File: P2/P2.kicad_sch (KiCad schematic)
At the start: 16 parts, among them J1 Power, J2 Digital/PWM, J3 Analog, J4 Digital/PWM, SW1 SW_Rotary_2x6, U2 LM393

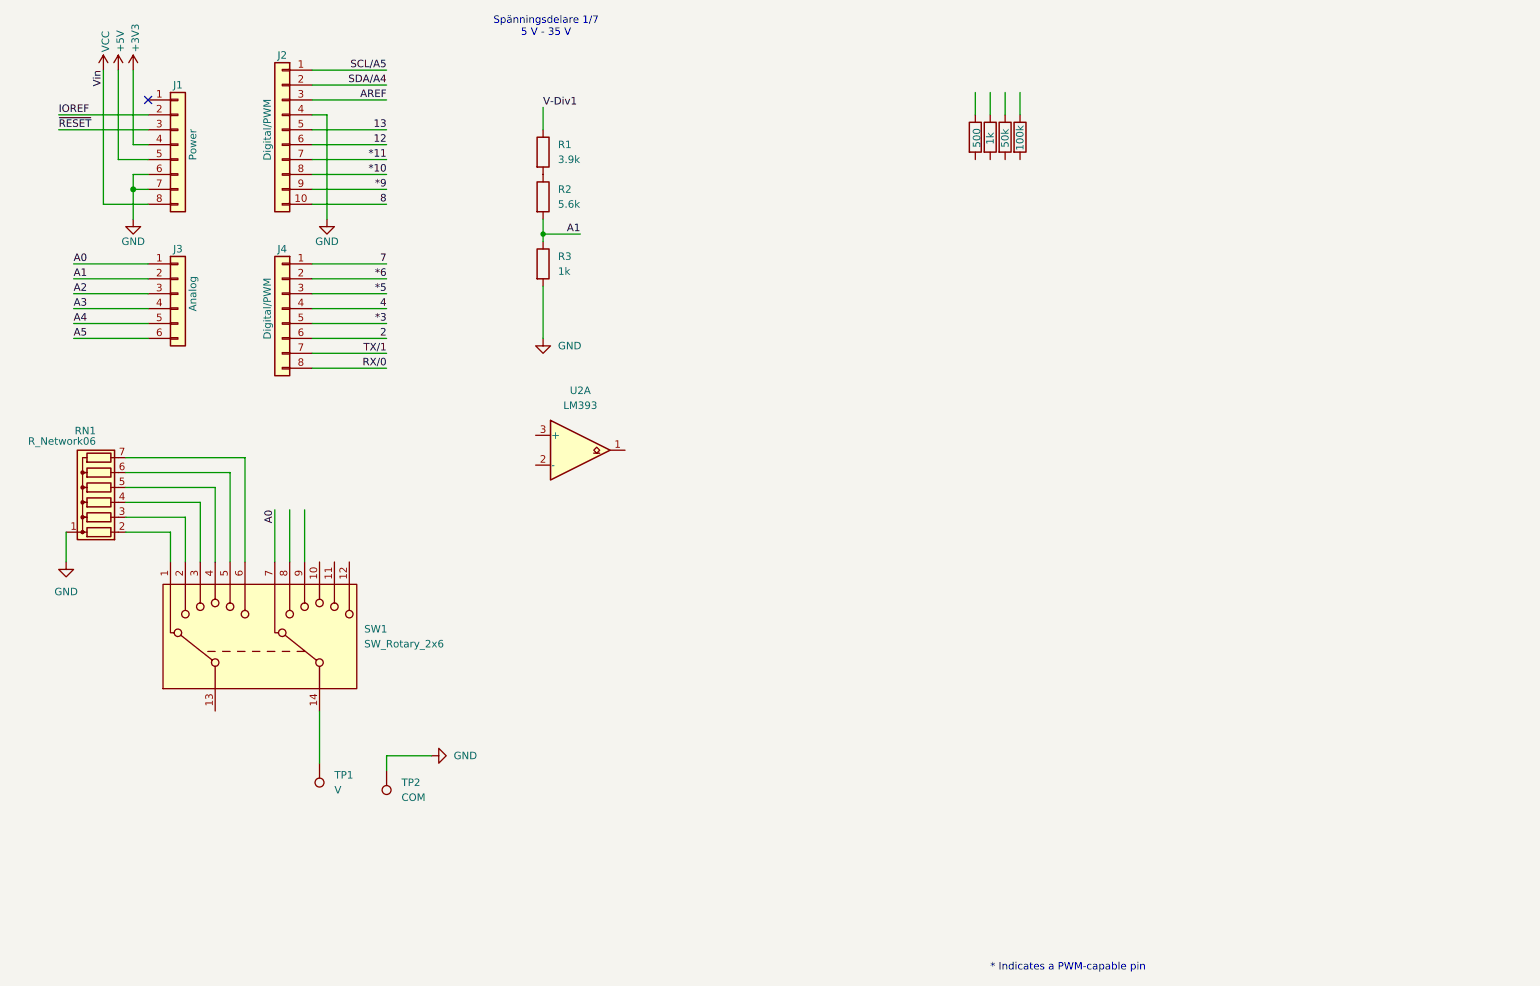
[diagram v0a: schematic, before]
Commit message: Adds rounding and formatting data for P2
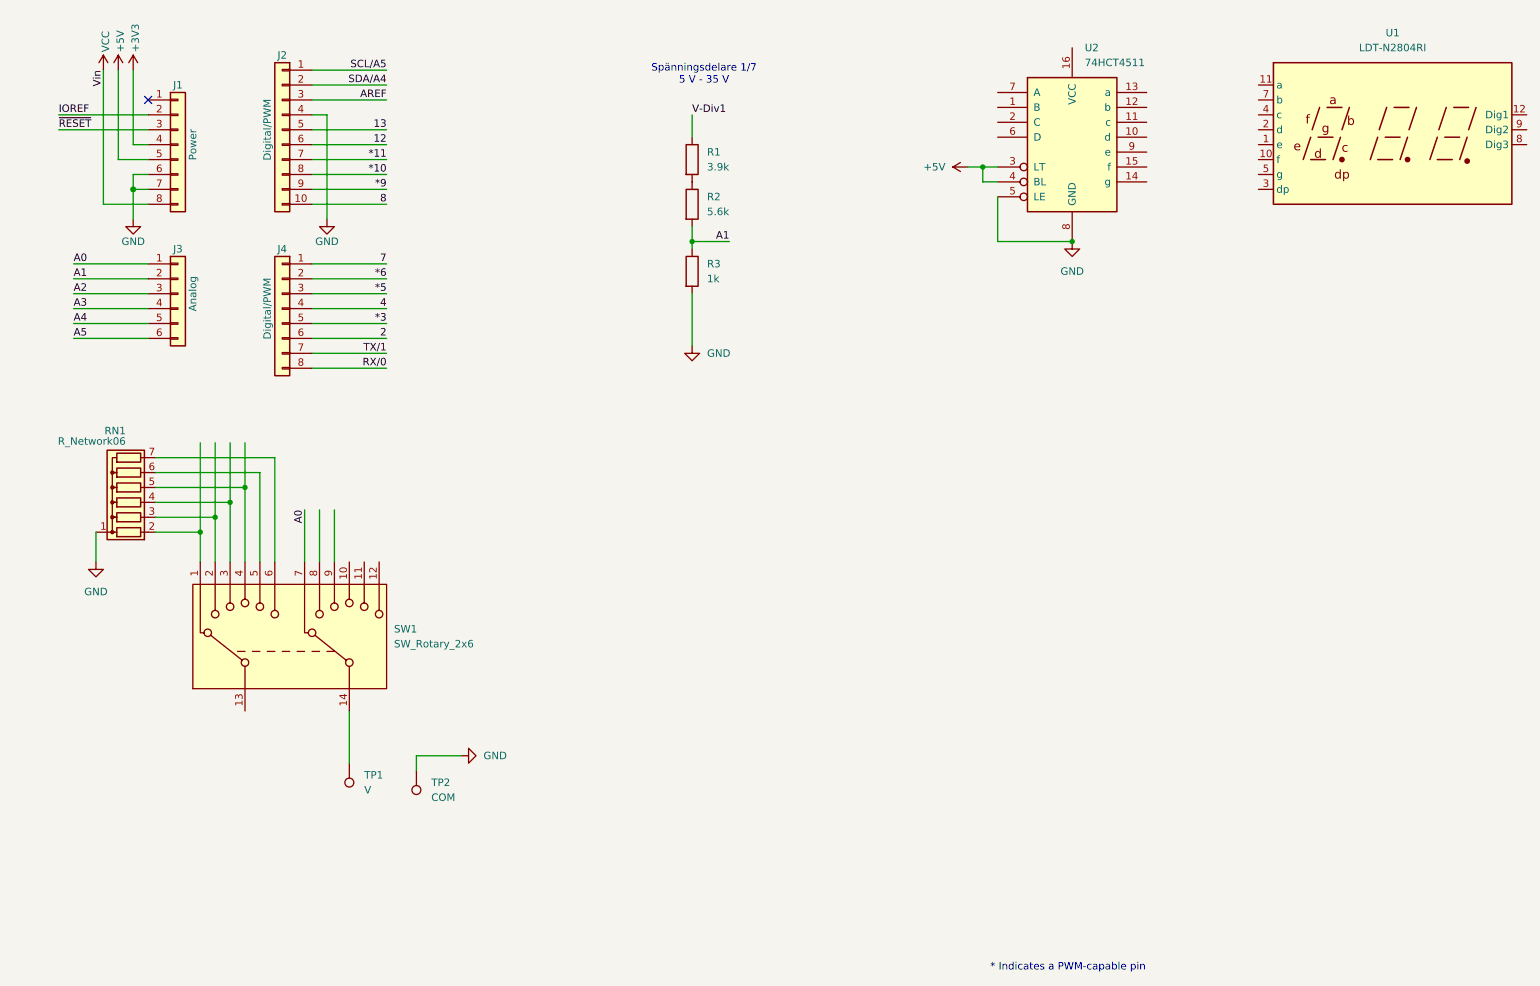
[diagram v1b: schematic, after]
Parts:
- removed R4: 500, symbol Device:R
- removed R5: 1k, symbol Device:R
- removed R6: 50k, symbol Device:R
- removed R7: 100k, symbol Device:R
- removed U2: LM393, symbol Comparator:LM393
- added U1: LDT-N2804RI, Display_7Segment:CA56-12SRWA, symbol joel_library:LDT-N2804RI
- added U2: 74HCT4511, symbol joel_library:74HCT4511
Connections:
- net +5V: now also U2.3 (LT), U2.4 (BL)
- net GND: now also U2.5 (LE), U2.8 (GND)
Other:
- moved on the sheet: R1, R2, R3, RN1, SW1, TP1, TP2
